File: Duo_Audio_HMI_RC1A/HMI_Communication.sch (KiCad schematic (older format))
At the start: 26 parts, among them Q1 BC847, Q2 BC847, U4 SN75176BDR

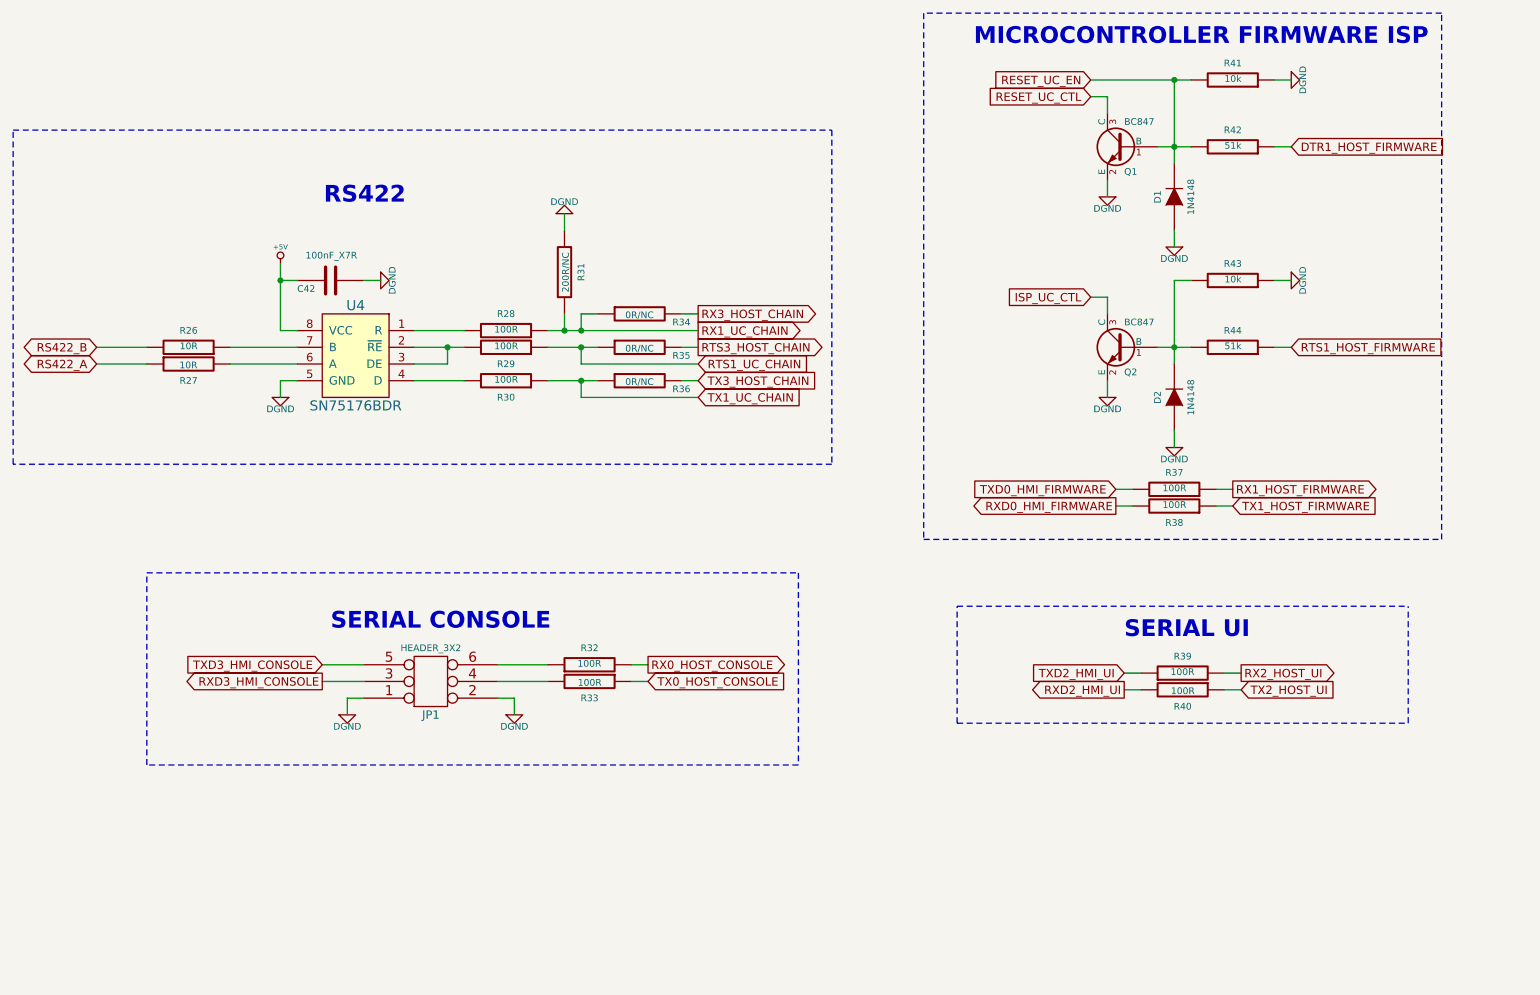
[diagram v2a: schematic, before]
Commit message: Major changes on hardware architecture. Migrating to a HMI separated board. HMI schematic finalized.
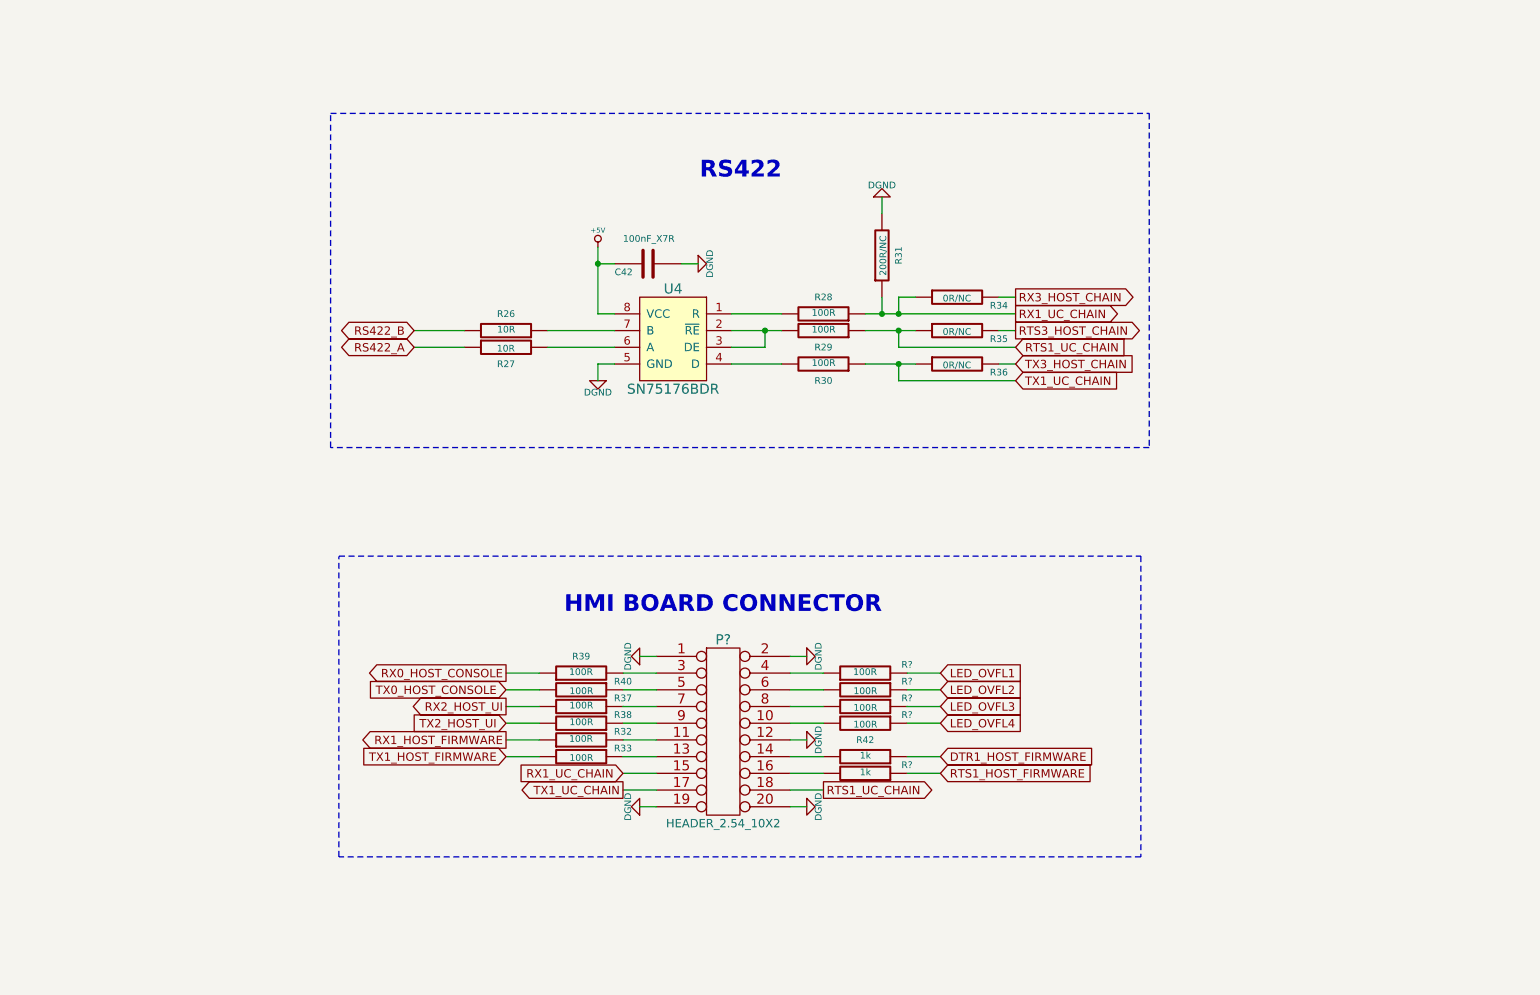
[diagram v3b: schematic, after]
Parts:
- removed D1, D2: 1N4148, SOD323, symbol DIODE
- removed JP1: HEADER_3X2, PIN_ARRAY_3X2, symbol CONN_3X2
- removed Q1, Q2: BC847, SOT23, symbol BC850
- removed R41, R43: 10k, SM0603, symbol R
- removed R44: 51k, SM0603, symbol R
- added P?: HEADER_2.54_10X2, symbol CONN_10X2
- added R? (x4): 100R, SM0603, symbol R
- added R?: 1k, SM0603, symbol R
- R42: value 51k -> 1k
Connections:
- net RXD0_HMI_FIRMWARE is gone; now on net TX2_HOST_UI: R38.2
- net RXD2_HMI_UI is gone; now on net TX0_HOST_CONSOLE: R40.2
- net TXD0_HMI_FIRMWARE is gone; now on net RX2_HOST_UI: R37.2
- net TXD2_HMI_UI is gone; now on net RX0_HOST_CONSOLE: R39.1
- net DGND: now also P?.1 (P1), P?.12 (P12), P?.19 (P19), P?.2 (P2), P?.20 (P20)
- net RTS1_HOST_FIRMWARE: now also R?.1
- net RTS1_UC_CHAIN: now also P?.18 (P18)
- net RX0_HOST_CONSOLE: no longer R32.2
- net RX1_HOST_FIRMWARE: now also R32.1; no longer R37.1
- net RX1_UC_CHAIN: now also P?.15 (P15)
- net RX2_HOST_UI: no longer R39.2
- net TX0_HOST_CONSOLE: no longer R33.1
- net TX1_HOST_FIRMWARE: now also R33.2; no longer R38.1
- net TX1_UC_CHAIN: now also P?.17 (P17)
- net TX2_HOST_UI: no longer R40.1
- net RESET_UC_EN: no longer names the net of R42.2
- net RESET_UC_EN: now also P?.14 (P14)
- new net: P?.11 (P11), R32.2
- new net: P?.13 (P13), R33.1
- new net: P?.3 (P3), R39.2
- new net: P?.5 (P5), R40.1
- new net: P?.7 (P7), R37.1
- new net: P?.9 (P9), R38.1
- new net: P?.10 (P10), R?.2
- new net: P?.16 (P16), R?.2
- new net: P?.4 (P4), R?.1
- new net: P?.6 (P6), R?.2
- new net: P?.8 (P8), R?.2
- new net LED_OVFL1: R?.2
- new net LED_OVFL2: R?.1
- new net LED_OVFL3: R?.1
- new net LED_OVFL4: R?.1
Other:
- note added: "HMI BOARD CONNECTOR"
- note removed: "MICROCONTROLLER FIRMWARE ISP"
- note removed: "SERIAL CONSOLE"
- note removed: "SERIAL UI"
- moved on the sheet: C42, R26, R27, R28, R29, R30, R31, R32, R33, R34, R35, R36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
